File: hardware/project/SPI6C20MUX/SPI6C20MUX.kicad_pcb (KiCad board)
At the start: 2 copper layers, 160 x 100 mm, 93 parts, among them J201 5499141-4, J301 Conn_01x06, J302 Conn_02x08_Odd_Even, K201 HE3621A0510, K202 HE3621A0510, K203 HE3621A0510, K204 HE3621A0510, K205 HE3621A0510, K206 HE3621A0510, K207 HE3621A0510, K208 HE3621A0510, K209 HE3621A0510, K210 HE3621A0510, K211 HE3621A0510, K212 HE3621A0510, K213 HE3621A0510, K214 HE3621A0510, K215 HE3621A0510, K216 HE3621A0510, K217 HE3621A0510, K218 HE3621A0510, K219 HE3621A0510, K220 HE3621A0510, K221 HE3621A0510, K222 HE3621A0510, K223 HE3621A0510, K224 HE3621A0510, K225 HE3621A0510, K226 HE3621A0510, K227 HE3621A0510, K228 HE3621A0510, K229 HE3621A0510, K230 HE3621A0510, K231 HE3621A0510, K232 HE3621A0510, K233 HE3621A0510, K234 HE3621A0510, K235 HE3621A0510, K236 HE3621A0510, K237 HE3621A0510, K238 HE3621A0510, K239 HE3621A0510, K240 HE3621A0510, K241 HE3621A0510, K242 HE3621A0510, K243 HE3621A0510, K244 HE3621A0510, K245 HE3621A0510, K246 HE3621A0510, K247 HE3621A0510, K248 HE3621A0510, K249 HE3621A0510, K250 HE3621A0510, K251 HE3621A0510, K252 HE3621A0510, K253 HE3621A0510, K254 HE3621A0510, K255 HE3621A0510, K256 HE3621A0510, K257 HE3621A0510, K258 HE3621A0510, K259 HE3621A0510, K260 HE3621A0510, K261 HE3621A0510, K262 HE3621A0510, K263 HE3621A0510, K264 HE3621A0510, K265 HE3621A0510, K266 HE3621A0510, U201 MCZ33996, U202 MCZ33996, U203 MCZ33996, U204 MCZ33996, U205 MCZ33996, U401 LM1117MPX-3.3

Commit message: SPI6C20MUX layout done, bug fixes in ETH6C20MUX layout.
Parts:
- C401, C402, C403, C404: moved to B.Cu
- moved U203 176.5 mm to (121.8, 119.4)
- moved U202 173.5 mm to (103.9, 119.4)
- moved U205 172.6 mm to (157.3, 119.4)
- moved U201 156.3 mm to (86.2, 119.4)
- moved U204 155.4 mm to (139.6, 119.4)
- moved C206 145.2 mm to (77.6, 117.5), turned to 180 degrees
- moved C404 143.3 mm to (182.5, 117.1), turned to 180 degrees
- moved C403 139.9 mm to (187.6, 117.1)
- moved C207 139.0 mm to (95.4, 117.5), turned to 180 degrees
- moved C205 138.6 mm to (148.6, 115.8), turned to 180 degrees
- moved C204 134.0 mm to (131.1, 115.8), turned to 180 degrees
- moved C209 132.5 mm to (131.1, 117.5), turned to 180 degrees
- moved C201 132.3 mm to (77.6, 115.8), turned to 180 degrees
- moved C401 128.2 mm to (182.5, 133.2), turned to 180 degrees
- moved C202 126.4 mm to (95.4, 115.8), turned to 180 degrees
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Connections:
- net /Relays/RELAY2A renamed /Relays/RELAY22A
- net /Relays/RELAY2B renamed /Relays/RELAY22B
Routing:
- net /Relays/PIN21C: track 0.00 -> 450.2 mm
- net /Relays/PIN21B: track 0.00 -> 435.5 mm
- net /Relays/PIN21A: track 0.00 -> 428.7 mm
- net /Relays/PIN40: track 0.00 -> 131.5 mm
- net /Connector/RELAY2_SCLK: track 0.00 -> 126.5 mm, vias 0 -> 11
- net /Connector/RELAY2_SO: track 0.00 -> 123.0 mm, vias 0 -> 9
- net /Relays/PIN33: track 0.00 -> 116.5 mm, vias 0 -> 1
- net /Connector/RELAY2_SI: track 0.00 -> 114.6 mm, vias 0 -> 7
- net /Relays/PIN39: track 0.00 -> 113.7 mm
- net /Relays/PIN32: track 0.00 -> 104.6 mm, vias 0 -> 1
- net /Connector/RELAY2_~RST: track 0.00 -> 102.2 mm, vias 0 -> 9
- net /Relays/PIN38: track 0.00 -> 101.5 mm
- net /Relays/PIN26: track 0.00 -> 101.3 mm, vias 0 -> 1
- net /Relays/RELAY38C: track 0.00 -> 98.0 mm
- net /Relays/RELAY38B: track 0.00 -> 96.7 mm
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- added copper zone on B.Cu, net +3V3
- added copper zone on F.Cu, net +3V3
- added copper zone on Power, net +3V3
- added copper zone on B.Cu, net +5V
- added copper zone on F.Cu, net +5V
- added copper zone on Power, net +5V
- added copper zone on B.Cu, net GND
- added copper zone on F.Cu, net GND
- added copper zone on GND, net GND
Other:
- copper layers 2 -> 4
- net class Default: clearance 0.2 -> 0.127; trace_width 0.25 -> 0.127
- net class Relay signal 100V added: clearance 0.3, trace_width 0.381, via_dia 0.8, via_drill 0.4
- rule pad_to_mask_clearance: 0.051 -> 0
- rule trace_clearance: 0.2 -> 0.127
- rule trace_min: 0.2 -> 0.1
- rule via_min_drill: 0.3 -> 0.2
- rule via_min_size: 0.4 -> 0.5
- board text added: "1"
- board text added: "2"
- board text added: "21A"
- board text added: "21B"
- board text added: "21C"
- board text added: "22A"
- board text added: "22B"
- board text added: "22C"
- board text added: "23A"
- board text added: "23B"
- board text added: "23C"
- board text added: "24A"
- board text added: "24B"
- board text added: "24C"
- board text added: "25A"
- board text added: "25B"
- board text added: "25C"
- board text added: "26A"
- board text added: "26B"
- board text added: "26C"
- board text added: "27A"
- board text added: "27B"
- board text added: "27C"
- board text added: "28A"
- board text added: "28B"
- board text added: "28C"
- board text added: "29A"
- board text added: "29B"
- board text added: "29C"
- board text added: "3"
- board text added: "30A"
- board text added: "30B"
- board text added: "30C"
- board text added: "31A"
- board text added: "31B"
- board text added: "31C"
- board text added: "32A"
- board text added: "32B"
- board text added: "32C"
- board text added: "33A"
- board text added: "33B"
- board text added: "33C"
- board text added: "34A"
- board text added: "34B"
- board text added: "34C"
- board text added: "35A"
- board text added: "35B"
- board text added: "35C"
- board text added: "36A"
- board text added: "36B"
- board text added: "36C"
- board text added: "37A"
- board text added: "37B"
- board text added: "37C"
- board text added: "38A"
- board text added: "38B"
- board text added: "38C"
- board text added: "39A"
- board text added: "39B"
- board text added: "39C"
- board text added: "4"
- board text added: "40A"
- board text added: "40B"
- board text added: "40C"
- board text added: "AA"
- board text added: "AF"
- board text added: "BB"
- board text added: "BE"
- board text added: "CC"
- board text added: "CD"

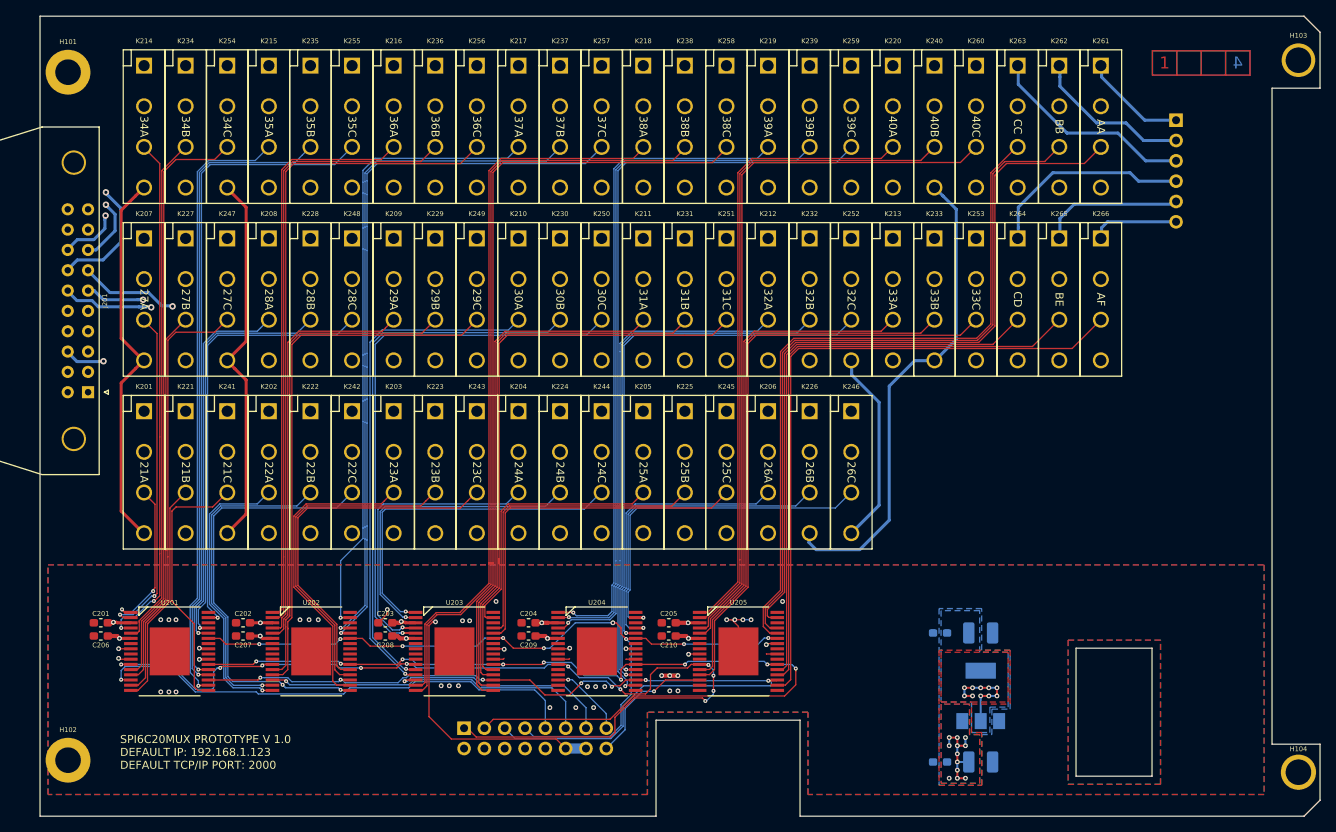
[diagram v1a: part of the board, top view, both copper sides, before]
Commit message: Added firmware software, based on zephyr OS.
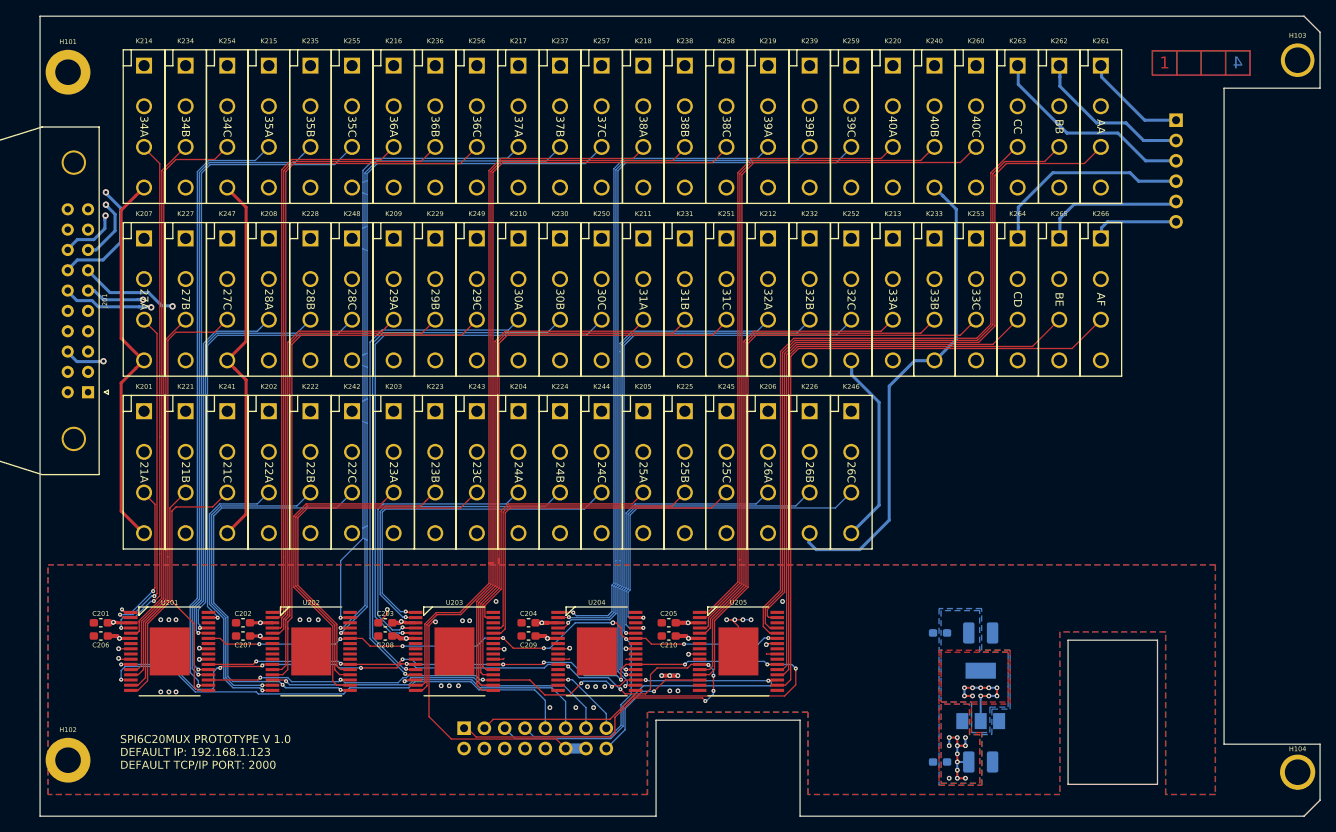
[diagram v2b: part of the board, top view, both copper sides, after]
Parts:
- moved H103 0.10 mm to (227.2, 45.5)
- moved H104 0.10 mm to (227.2, 134.5)
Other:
- outline, holes or cut-outs redrawn
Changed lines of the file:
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@@
   )
   (module MountingHole:MountingHole_3.2mm_M3_DIN965_Pad (layer Top)
-    (at 227.3 134.5)
+    (at 227.2 134.5)
     (descr "Mounting Hole 3.2mm, M3, DIN965")
     (tags "mounting hole 3.2mm m3 din965")
@@
   )
   (module MountingHole:MountingHole_3.2mm_M3_DIN965_Pad (layer Top)
-    (at 227.3 45.5)
+    (at 227.2 45.5)
     (descr "Mounting Hole 3.2mm, M3, DIN965")
     (tags "mounting hole 3.2mm m3 din965")
@@
   (gr_line (start 228 140) (end 165 140) (layer Edge.Cuts) (width 0.05))
   (gr_line (start 230 138) (end 228 140) (layer Edge.Cuts) (width 0.05))
-  (gr_line (start 209 119) (end 199.5 119) (layer Edge.Cuts) (width 0.05))
-  (gr_line (start 209 135) (end 209 119) (layer Edge.Cuts) (width 0.05))
-  (gr_line (start 199.5 135) (end 209 135) (layer Edge.Cuts) (width 0.05))
-  (gr_line (start 199.5 135) (end 199.5 119) (layer Edge.Cuts) (width 0.05))
+  (gr_line (start 209.677 118) (end 198.5 118) (layer Edge.Cuts) (width 0.05))
+  (gr_line (start 209.678 136.017) (end 209.677 118) (layer Edge.Cuts) (width 0.05))
+  (gr_line (start 198.501 136.017) (end 209.677 136.017) (layer Edge.Cuts) (width 0.05))
+  (gr_line (start 198.501 136.017) (end 198.5 118) (layer Edge.Cuts) (width 0.05))
   (gr_line (start 147 140) (end 70 140) (layer Edge.Cuts) (width 0.05))
   (gr_line (start 165 128) (end 147 128) (layer Edge.Cuts) (width 0.05))
   (gr_line (start 165 140) (end 165 128) (layer Edge.Cuts) (width 0.05))
   (gr_line (start 147 140) (end 147 128) (layer Edge.Cuts) (width 0.05))
-  (gr_line (start 224 131) (end 224 49) (layer Edge.Cuts) (width 0.05))
+  (gr_line (start 218 131) (end 218 49) (layer Edge.Cuts) (width 0.05))
   (gr_line (start 230 42) (end 230 49) (layer Edge.Cuts) (width 0.05))
   (gr_line (start 230 131) (end 230 138) (layer Edge.Cuts) (width 0.05))
-  (gr_line (start 230 131) (end 224 131) (layer Edge.Cuts) (width 0.05))
-  (gr_line (start 230 49) (end 224 49) (layer Edge.Cuts) (width 0.05))
+  (gr_line (start 230 131) (end 218 131) (layer Edge.Cuts) (width 0.05))
+  (gr_line (start 230 49) (end 218 49) (layer Edge.Cuts) (width 0.05))
   (gr_line (start 228 40) (end 70 40) (layer Edge.Cuts) (width 0.05))
   (gr_line (start 70 40) (end 70 140) (layer Edge.Cuts) (width 0.05))
@@
   (segment (start 91.440071 102.361929) (end 91.440071 113.415905) (width 0.127) (layer Bottom) (net 107))
   (segment (start 91.440071 113.415905) (end 93.218 115.193834) (width 0.127) (layer Bottom) (net 107))
-  (zone (net 3) (net_name +5V) (layer Power) (hatch edge 0.508)
-    (connect_pads yes (clearance 0.127))
-    (min_thickness 0.12)
-    (fill yes (arc_segments 32) (thermal_gap 0.127) (thermal_bridge_width 0.508) (smoothing chamfer) (radius 0.254))
-    (polygon
-      (pts
-        (xy 205.232 53.868717) (xy 78.994 53.868717) (xy 78.994 70.378717) (xy 205.232 70.378717) (xy 205.232 75.458717)
-        (xy 78.994 75.458717) (xy 78.994 91.968717) (xy 173.863 91.968717) (xy 173.863 97.048717) (xy 78.994 97.048717)
-        (xy 78.994 108.585) (xy 223.012 108.585) (xy 223.012 137.287) (xy 165.989 137.287) (xy 165.989 127)
-        (xy 145.923 127) (xy 145.923 137.287) (xy 70.993 137.287) (xy 70.993 48.788717) (xy 205.232 48.788717)
-      )
-    )
-    (polygon
-      (pts
-        (xy 198.501 117.983) (xy 198.501 136.017) (xy 210.058 136.017) (xy 210.058 117.983)
-      )
-    )
-    (polygon
-      (pts
-        (xy 78.486 110.617) (xy 78.486 116.586) (xy 182.372 116.586) (xy 182.372 125.984) (xy 186.182 125.984)
-        (xy 186.182 129.794) (xy 193.04 129.794) (xy 193.04 110.617)
-      )
-    )
-  )
-  (zone (net 1) (net_name GND) (layer GND) (hatch edge 0.508)
-    (connect_pads yes (clearance 0.127))
-    (min_thickness 0.123)
-    (fill yes (arc_segments 32) (thermal_gap 0.508) (thermal_bridge_width 0.508) (smoothing chamfer) (radius 0.254))
-    (polygon
-      (pts
-        (xy 223.012 137.287) (xy 165.989 137.287) (xy 165.989 127) (xy 145.923 127) (xy 145.923 137.287)
-        (xy 70.993 137.287) (xy 70.993 108.585) (xy 223.012 108.585)
-      )
-    )
-    (polygon
-      (pts
-        (xy 198.501 117.983) (xy 198.501 136.017) (xy 210.058 136.017) (xy 210.058 117.983)
-      )
-    )
-  )
   (zone (net 2) (net_name +3V3) (layer Power) (hatch edge 0.508)
     (connect_pads yes (clearance 0.127))
@@
     )
   )
-  (zone (net 1) (net_name GND) (layer Bottom) (hatch edge 0.508)
-    (connect_pads (clearance 0.127))
-    (min_thickness 0.12)
-    (fill yes (arc_segments 32) (thermal_gap 0.127) (thermal_bridge_width 0.508) (smoothing chamfer) (radius 0.254))
-    (polygon
-      (pts
-        (xy 223.012 137.287) (xy 165.989 137.287) (xy 165.989 127) (xy 145.923 127) (xy 145.923 137.287)
-        (xy 70.993 137.287) (xy 70.993 108.585) (xy 223.012 108.585)
-      )
-    )
-    (polygon
-      (pts
-        (xy 182.372 114.046) (xy 182.372 136.144) (xy 187.706 136.144) (xy 187.706 129.794) (xy 188.976 129.794)
-        (xy 188.976 126.619) (xy 191.262 126.619) (xy 191.262 119.253) (xy 187.706 119.253) (xy 187.706 114.046)
-      )
-    )
-    (polygon
-      (pts
-        (xy 198.501 117.983) (xy 198.501 136.017) (xy 210.058 136.017) (xy 210.058 117.983)
-      )
-    )
-  )
   (zone (net 3) (net_name +5V) (layer Top) (hatch edge 0.508)
     (priority 1)
@@
     (polygon
       (pts
-        (xy 223.012 137.287) (xy 165.989 137.287) (xy 165.989 127) (xy 145.923 127) (xy 145.923 137.287)
-        (xy 70.993 137.287) (xy 70.993 108.585) (xy 223.012 108.585)
+        (xy 197.485 116.967) (xy 197.485 137.287) (xy 165.989 137.287) (xy 165.989 127) (xy 145.923 127)
+        (xy 145.923 137.287) (xy 70.993 137.287) (xy 70.993 108.585) (xy 216.916 108.585) (xy 216.916 137.287)
+        (xy 210.693 137.287) (xy 210.693 116.967)
       )
     )
@@
       )
     )
+  )
+  (zone (net 1) (net_name GND) (layer Bottom) (hatch edge 0.508)
+    (connect_pads (clearance 0.127))
+    (min_thickness 0.12)
+    (fill yes (arc_segments 32) (thermal_gap 0.127) (thermal_bridge_width 0.508) (smoothing chamfer) (radius 0.254))
+    (polygon
+      (pts
+        (xy 197.485 116.967) (xy 197.485 137.287) (xy 165.989 137.287) (xy 165.989 127) (xy 145.923 127)
+        (xy 145.923 137.287) (xy 70.993 137.287) (xy 70.993 108.585) (xy 216.916 108.585) (xy 216.916 137.287)
+        (xy 210.693 137.287) (xy 210.693 116.967)
+      )
+    )
+    (polygon
+      (pts
+        (xy 182.372 114.046) (xy 182.372 136.144) (xy 187.706 136.144) (xy 187.706 129.794) (xy 188.976 129.794)
+        (xy 188.976 126.619) (xy 191.262 126.619) (xy 191.262 119.253) (xy 187.706 119.253) (xy 187.706 114.046)
+      )
+    )
+  )
+  (zone (net 3) (net_name +5V) (layer Power) (hatch edge 0.508)
+    (connect_pads yes (clearance 0.127))
+    (min_thickness 0.12)
+    (fill yes (arc_segments 32) (thermal_gap 0.127) (thermal_bridge_width 0.508) (smoothing chamfer) (radius 0.254))
+    (polygon
+      (pts
+        (xy 197.485 116.967) (xy 197.485 137.287) (xy 165.989 137.287) (xy 165.989 127) (xy 145.923 127)
+        (xy 145.923 137.287) (xy 70.993 137.287) (xy 70.993 48.788717) (xy 205.232 48.788717) (xy 205.232 53.868717)
+        (xy 78.994 53.868717) (xy 78.994 70.378717) (xy 205.232 70.378717) (xy 205.232 75.458717) (xy 78.994 75.458717)
+        (xy 78.994 91.968717) (xy 173.863 91.968717) (xy 173.863 97.048717) (xy 78.994 97.048717) (xy 78.994 108.585)
+        (xy 216.916 108.585) (xy 216.916 137.287) (xy 210.693 137.287) (xy 210.693 116.967)
+      )
+    )
+    (polygon
+      (pts
+        (xy 78.486 110.617) (xy 78.486 116.586) (xy 182.372 116.586) (xy 182.372 125.984) (xy 186.182 125.984)
+        (xy 186.182 129.794) (xy 193.04 129.794) (xy 193.04 110.617)
+      )
+    )
+  )
+  (zone (net 1) (net_name GND) (layer GND) (hatch edge 0.508)
+    (connect_pads yes (clearance 0.127))
+    (min_thickness 0.123)
+    (fill yes (arc_segments 32) (thermal_gap 0.508) (thermal_bridge_width 0.508) (smoothing chamfer) (radius 0.254))
     (polygon
       (pts
-        (xy 198.501 117.983) (xy 198.501 136.017) (xy 210.058 136.017) (xy 210.058 117.983)
+        (xy 197.485 116.967) (xy 197.485 137.287) (xy 165.989 137.287) (xy 165.989 127) (xy 145.923 127)
+        (xy 145.923 137.287) (xy 70.993 137.287) (xy 70.993 108.585) (xy 216.916 108.585) (xy 216.916 137.287)
+        (xy 210.693 137.287) (xy 210.693 116.967)
       )
     )

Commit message: Small updates in PCB design.
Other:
- outline, holes or cut-outs redrawn
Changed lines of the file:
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@@
   (general
     (thickness 1.6)
-    (drawings 183)
+    (drawings 179)
     (tracks 1729)
     (zones 0)
@@
   )
   (gr_line (start 230 42) (end 228 40) (layer Edge.Cuts) (width 0.05))
-  (gr_line (start 228 140) (end 165 140) (layer Edge.Cuts) (width 0.05))
+  (gr_line (start 228 140) (end 166.1 140) (layer Edge.Cuts) (width 0.05))
   (gr_line (start 230 138) (end 228 140) (layer Edge.Cuts) (width 0.05))
-  (gr_line (start 209.677 118) (end 198.5 118) (layer Edge.Cuts) (width 0.05))
-  (gr_line (start 209.678 136.017) (end 209.677 118) (layer Edge.Cuts) (width 0.05))
-  (gr_line (start 198.501 136.017) (end 209.677 136.017) (layer Edge.Cuts) (width 0.05))
-  (gr_line (start 198.501 136.017) (end 198.5 118) (layer Edge.Cuts) (width 0.05))
   (gr_line (start 147 140) (end 70 140) (layer Edge.Cuts) (width 0.05))
-  (gr_line (start 165 128) (end 147 128) (layer Edge.Cuts) (width 0.05))
-  (gr_line (start 165 140) (end 165 128) (layer Edge.Cuts) (width 0.05))
-  (gr_line (start 147 140) (end 147 128) (layer Edge.Cuts) (width 0.05))
+  (gr_line (start 166.1 127.4) (end 147 127.4) (layer Edge.Cuts) (width 0.05))
+  (gr_line (start 166.1 140) (end 166.1 127.4) (layer Edge.Cuts) (width 0.05))
+  (gr_line (start 147 140) (end 147 127.4) (layer Edge.Cuts) (width 0.05))
   (gr_line (start 218 131) (end 218 49) (layer Edge.Cuts) (width 0.05))
   (gr_line (start 230 42) (end 230 49) (layer Edge.Cuts) (width 0.05))
@@
   (segment (start 133.036499 121.471501) (end 117.026501 121.471501) (width 0.127) (layer Bottom) (net 18))
   (segment (start 133.47699 121.03101) (end 133.036499 121.471501) (width 0.127) (layer Bottom) (net 18))
-  (via (at 115.833892 120.958716) (size 0.5) (drill 0.2) (layers Top Bottom) (net 18))
+  (via (at 115.833892 120.958716) (size 0.5) (drill 0.2) (layers Top Bottom) (net 18) (status 1000000))
   (segment (start 117.026501 121.471501) (end 116.513716 120.958716) (width 0.127) (layer Bottom) (net 18))
   (segment (start 116.513716 120.958716) (end 115.833892 120.958716) (width 0.127) (layer Bottom) (net 18))
@@
     (polygon
       (pts
-        (xy 197.485 116.967) (xy 197.485 137.287) (xy 165.989 137.287) (xy 165.989 127) (xy 145.923 127)
+        (xy 201.295 137.287) (xy 197.485 137.287) (xy 167.132 137.287) (xy 167.132 126.365) (xy 145.923 126.365)
         (xy 145.923 137.287) (xy 70.993 137.287) (xy 70.993 108.585) (xy 216.916 108.585) (xy 216.916 137.287)
-        (xy 210.693 137.287) (xy 210.693 116.967)
+        (xy 210.693 137.287) (xy 206.248 137.287)
       )
     )
@@
     (polygon
       (pts
-        (xy 197.485 116.967) (xy 197.485 137.287) (xy 165.989 137.287) (xy 165.989 127) (xy 145.923 127)
+        (xy 202.692 137.287) (xy 197.485 137.287) (xy 167.132 137.287) (xy 167.132 126.365) (xy 145.923 126.365)
         (xy 145.923 137.287) (xy 70.993 137.287) (xy 70.993 108.585) (xy 216.916 108.585) (xy 216.916 137.287)
-        (xy 210.693 137.287) (xy 210.693 116.967)
+        (xy 210.693 137.287) (xy 207.899 137.287)
       )
     )
@@
     (polygon
       (pts
-        (xy 197.485 116.967) (xy 197.485 137.287) (xy 165.989 137.287) (xy 165.989 127) (xy 145.923 127)
+        (xy 202.311 137.287) (xy 197.485 137.287) (xy 167.132 137.287) (xy 167.132 126.365) (xy 145.923 126.365)
         (xy 145.923 137.287) (xy 70.993 137.287) (xy 70.993 48.788717) (xy 205.232 48.788717) (xy 205.232 53.868717)
         (xy 78.994 53.868717) (xy 78.994 70.378717) (xy 205.232 70.378717) (xy 205.232 75.458717) (xy 78.994 75.458717)
         (xy 78.994 91.968717) (xy 173.863 91.968717) (xy 173.863 97.048717) (xy 78.994 97.048717) (xy 78.994 108.585)
-        (xy 216.916 108.585) (xy 216.916 137.287) (xy 210.693 137.287) (xy 210.693 116.967)
+        (xy 216.916 108.585) (xy 216.916 137.287) (xy 210.693 137.287) (xy 206.502 137.287)
       )
     )
@@
     (polygon
       (pts
-        (xy 197.485 116.967) (xy 197.485 137.287) (xy 165.989 137.287) (xy 165.989 127) (xy 145.923 127)
+        (xy 201.803 137.287) (xy 197.485 137.287) (xy 167.132 137.287) (xy 167.132 126.365) (xy 145.923 126.365)
         (xy 145.923 137.287) (xy 70.993 137.287) (xy 70.993 108.585) (xy 216.916 108.585) (xy 216.916 137.287)
-        (xy 210.693 137.287) (xy 210.693 116.967)
+        (xy 210.693 137.287) (xy 206.375 137.287)
       )
     )
